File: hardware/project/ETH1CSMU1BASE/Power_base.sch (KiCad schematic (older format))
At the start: 16 parts, among them Q401 IRFR5410, U404 LM1117IMP-3.3/NOPB, U405 TSR1-2450, U406 MAX5902

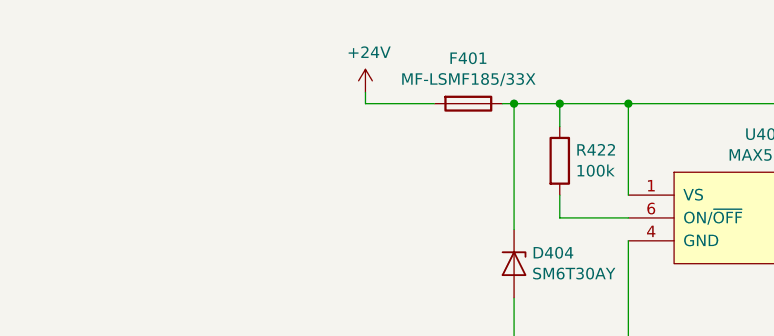
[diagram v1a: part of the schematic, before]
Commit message: Power supply design
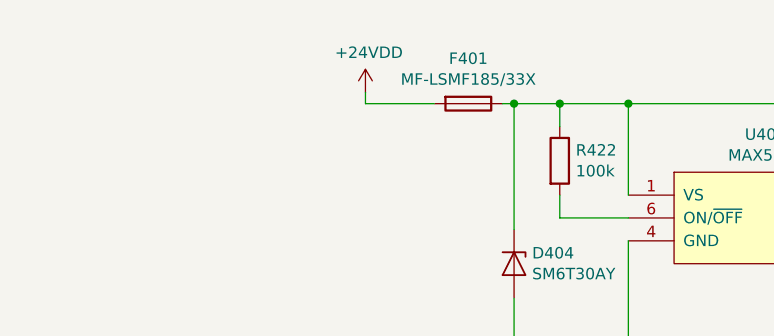
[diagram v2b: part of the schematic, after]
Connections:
- net +24V: no longer F401.2
- net +24VDD: now also F401.2
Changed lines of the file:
@@
 EESchema Schematic File Version 4
-LIBS:ETH1CSMU1BASE-cache
 EELAYER 30 0
 EELAYER END
@@
 	0    1    1    0
 $EndComp
-$Comp
-L power:+24V #PWR0108
-U 1 1 5D7B3705
-P 2200 2700
-F 0 "#PWR0108" H 2200 2550 50  0001 C CNN
-F 1 "+24V" H 2215 2873 50  0000 C CNN
-F 2 "" H 2200 2700 50  0001 C CNN
-F 3 "" H 2200 2700 50  0001 C CNN
-	1    2200 2700
-	1    0    0    -1
-$EndComp
 Wire Wire Line
 	4950 3350 5500 3350
@@
 Wire Wire Line
 	8400 2750 8750 2750
+$Comp
+L ETH1CSMU1:+24VDD #PWR0422
+U 1 1 5F53183E
+P 2200 2700
+F 0 "#PWR0422" H 2200 2550 50  0001 C CNN
+F 1 "+24VDD" H 2215 2873 50  0000 C CNN
+F 2 "" H 2200 2700 50  0001 C CNN
+F 3 "" H 2200 2700 50  0001 C CNN
+	1    2200 2700
+	1    0    0    -1
+$EndComp
 $EndSCHEMATC

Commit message: Footprint assigment
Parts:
- U405: footprint (none) -> ETH1CSMU1:TSR1
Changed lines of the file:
@@
 F 0 "U405" H 7250 3115 50  0000 C CNN
 F 1 "TSR1-2450" H 7250 3024 50  0000 C CNN
-F 2 "" H 7250 2800 50  0001 C CNN
+F 2 "ETH1CSMU1:TSR1" H 7250 2800 50  0001 C CNN
 F 3 "" H 7250 2800 50  0001 C CNN
 	1    7250 2800

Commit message: Footprint assignment
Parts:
- removed C415, C416: 10u/50V, Capacitor_SMD:C_2220_5650Metric_Pad1.97x5.40mm_HandSolder, symbol Device:C
- removed C417, C418: 22u/16V, Capacitor_SMD:C_2220_5650Metric_Pad1.97x5.40mm_HandSolder, symbol Device:C
- removed L402: TCK-141, ETH1CSMU1:TCK-141, symbol Device:L
- removed U404: LM1117IMP-3.3/NOPB, Package_TO_SOT_SMD:SOT-223-3_TabPin2, symbol Regulator_Linear:LM1117-3.3
- removed U405: TSR1-2450, ETH1CSMU1:TSR1, symbol ETH1CSMU1:TSR1-2450
- renumbered D404 to D301, D405 to D302, D403 to D303, F401 to F301, Q401 to Q301, R422 to R301, R423 to R302, R424 to R303, U406 to U301
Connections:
- net +24V: now also D303.1 (K), Q301.2 (D), R302.1, U301.2 (DRAIN)
- net +24VDD: no longer D303.1 (K), Q301.2 (D), R302.1, U301.2 (DRAIN)
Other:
- moved on the sheet: D301, D302, D303, F301, Q301, R301, R302, R303, U301
